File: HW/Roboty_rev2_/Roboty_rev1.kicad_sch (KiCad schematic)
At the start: 17 parts, among them J1 Micro_SD_Card, J4 Left_, J5 Right_, U5 LSM6DS3, U6 LIS2MDLTR

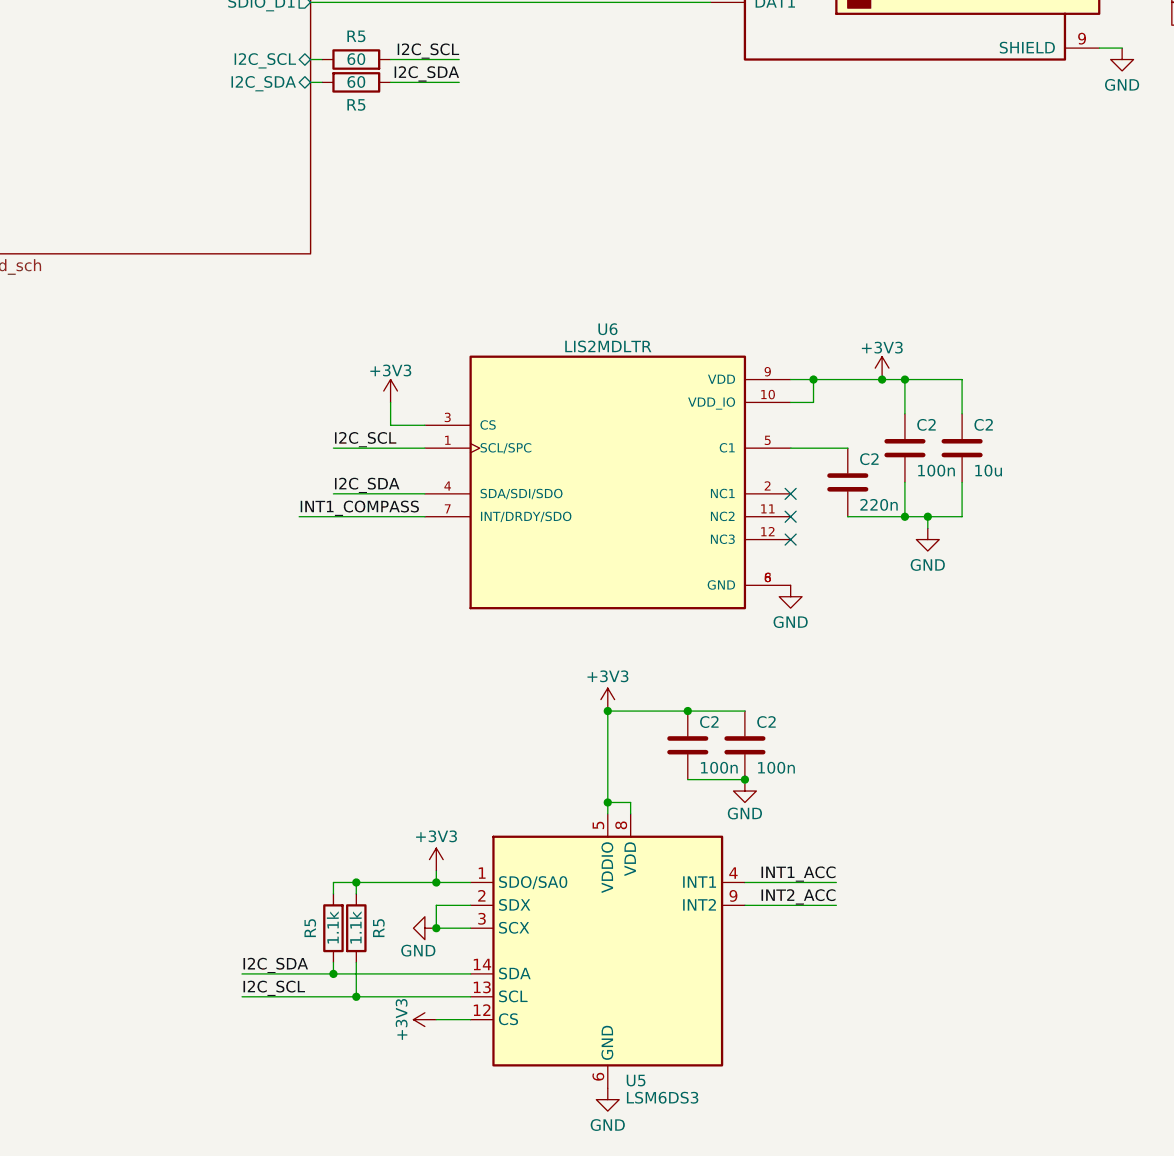
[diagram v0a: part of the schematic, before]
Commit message: add sd card file library+ new HW version
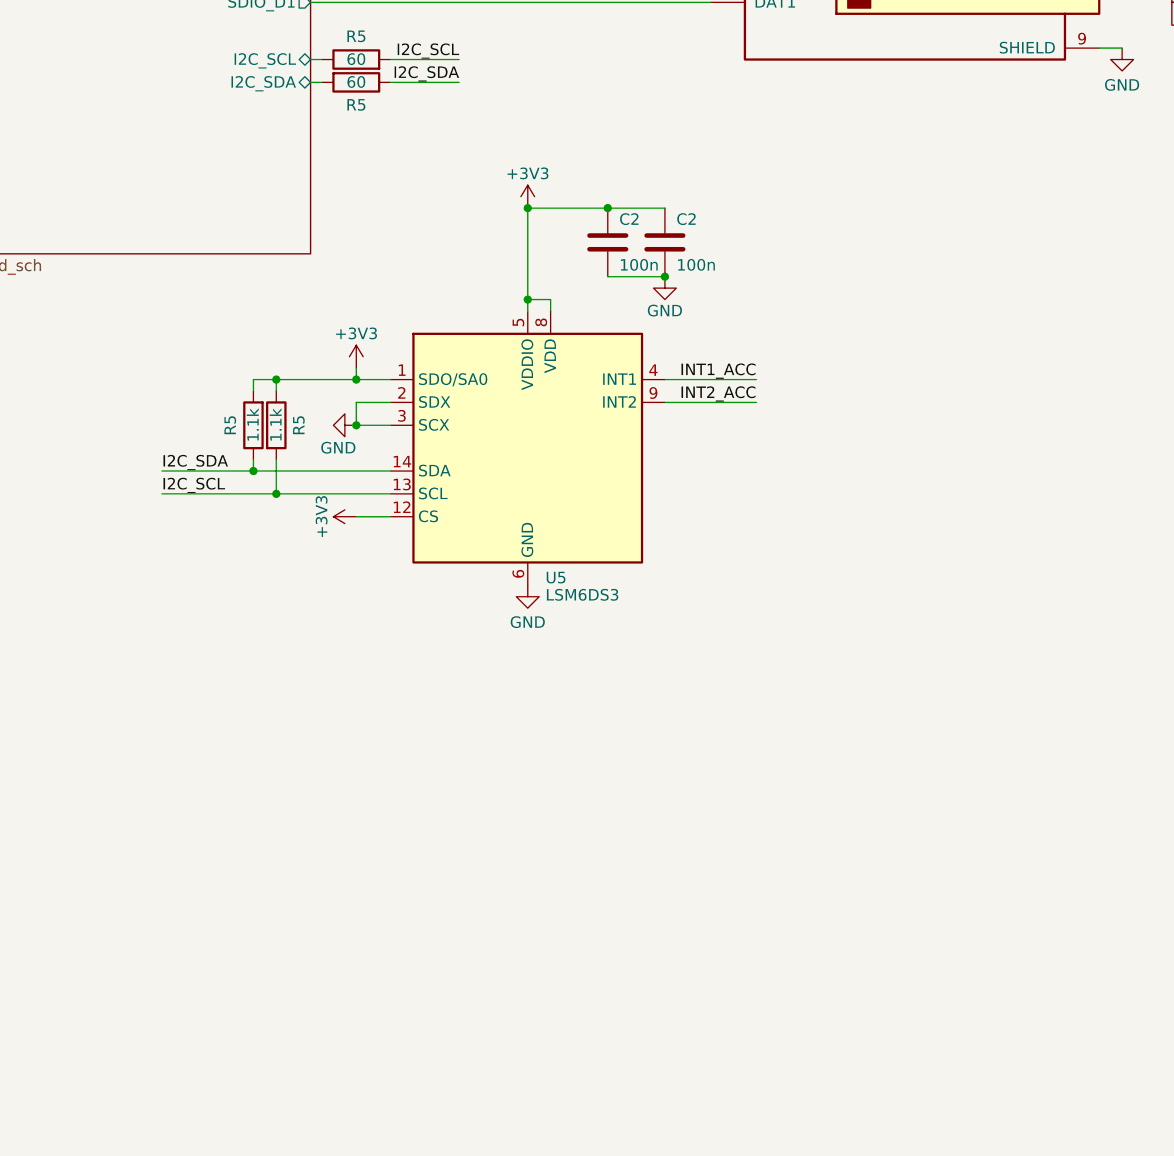
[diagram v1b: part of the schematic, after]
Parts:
- removed C2: 100n, Capacitor_SMD:C_0603_1608Metric, symbol Device:C
- removed C2: 10u, Capacitor_SMD:C_0603_1608Metric, symbol Device:C
- removed C2: 220n, Capacitor_SMD:C_0603_1608Metric, symbol Device:C
- removed U6: LIS2MDLTR, AREA_lib_composant:PQFN50P200X200X70-12N, symbol AREA_composant:LIS2MDLTR
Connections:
- no-connect marks 3 -> 0
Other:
- moved on the sheet: C2, R5, U5
